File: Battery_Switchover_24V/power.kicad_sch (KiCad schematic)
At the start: 20 parts, among them U12 L5973D, U13 AMS1117-3.3

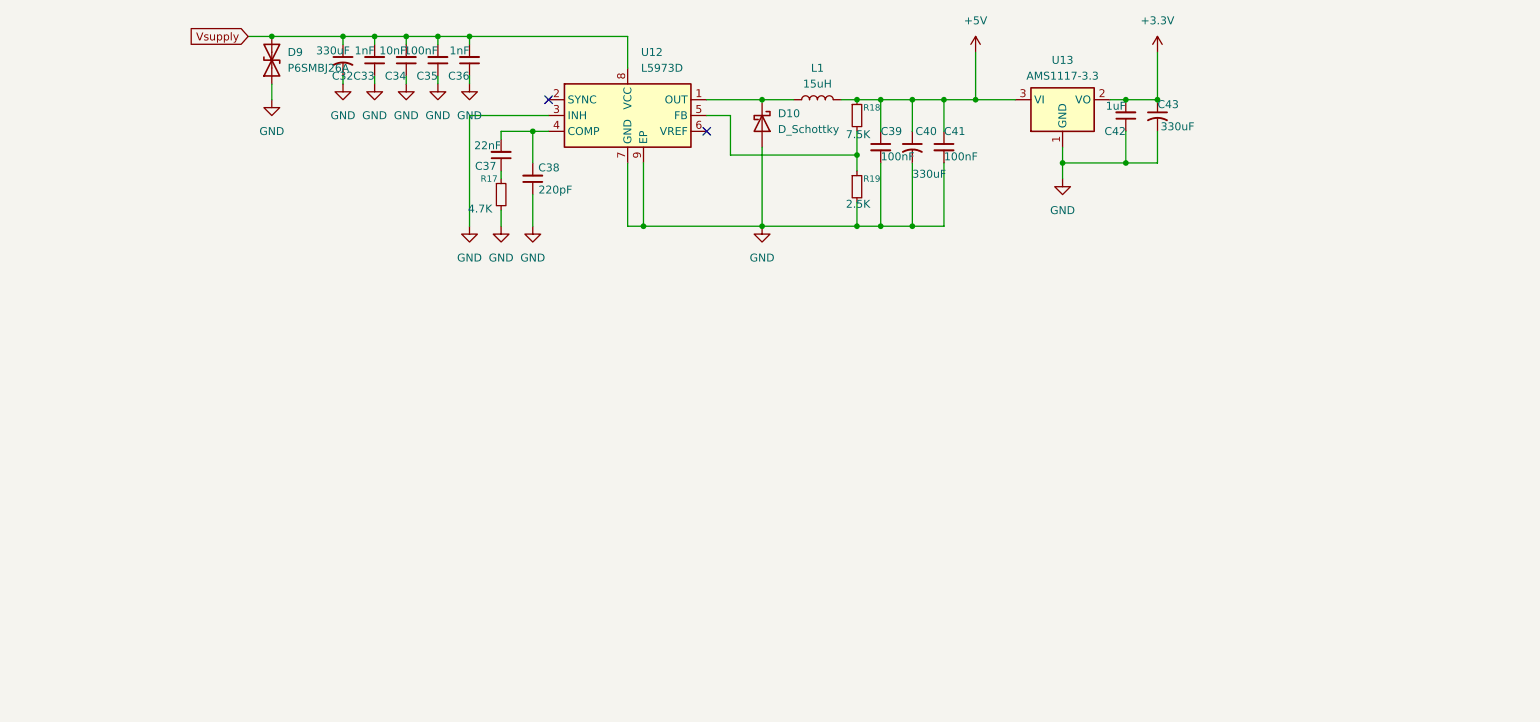
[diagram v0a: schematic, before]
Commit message: Added common mode chokes for input and output of the load fixed the corrupted board
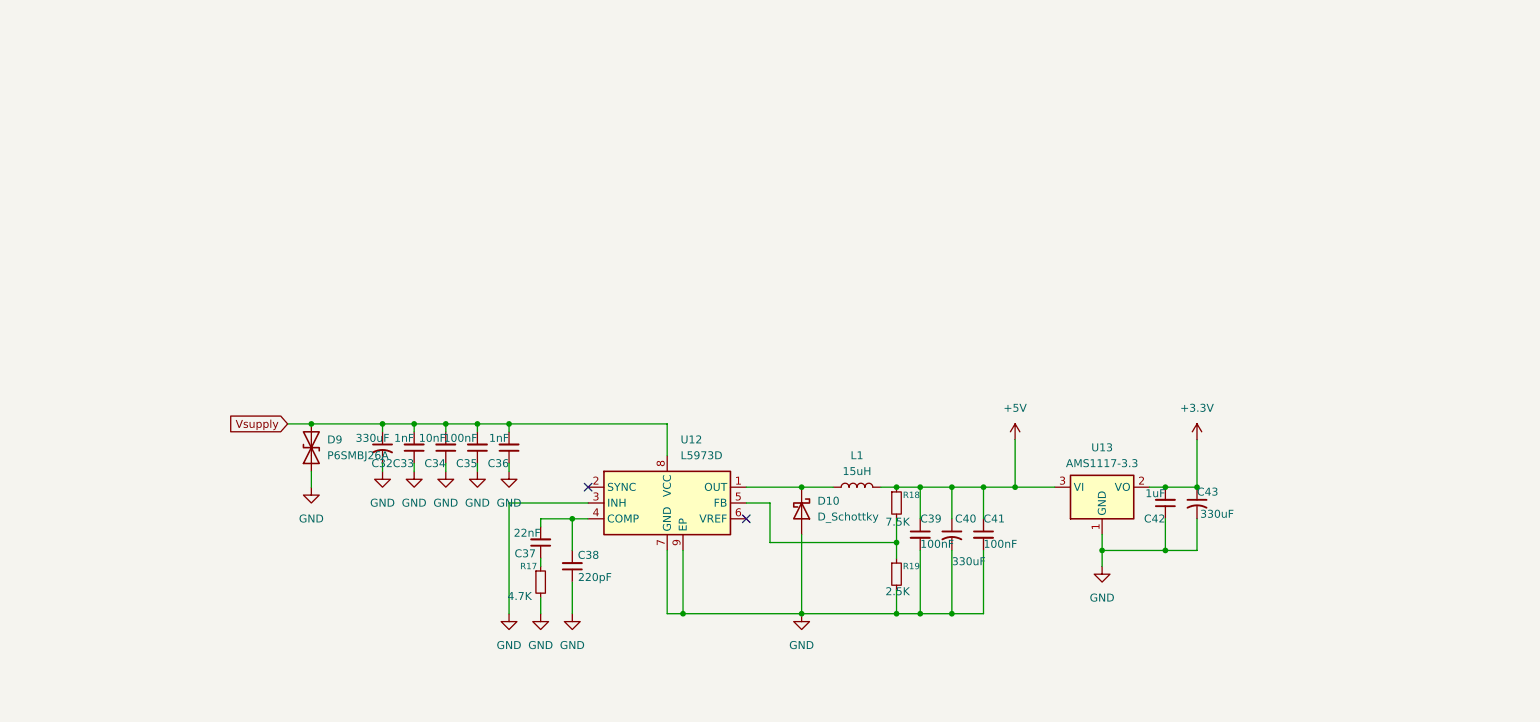
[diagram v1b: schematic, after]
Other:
- moved on the sheet: C32, C33, C34, C35, C36, C37, C38, C39, C40, C41, C42, C43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

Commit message: Added Footprints to the remaining parts calculated the current IC's resistance and capcitances
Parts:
- D10: footprint (none) -> Diode_SMD:D_SMA
- L1: footprint (none) -> footprints:IND_XAL6060_COC-L
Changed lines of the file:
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@@
 			)
 		)
-		(property "Footprint" ""
+		(property "Footprint" "footprints:IND_XAL6060_COC-L"
 			(at 161.29 113.03 0)
 			(effects
@@
 			)
 		)
-		(property "Footprint" ""
+		(property "Footprint" "Diode_SMD:D_SMA"
 			(at 152.4 116.84 0)
 			(effects
@@
 		)
 		(property "Footprint" "Capacitor_THT:CP_Radial_Tantal_D10.5mm_P5.00mm"
-			(at 85.09 106.68 0)
-			(effects
-				(font
+			(at 90.424 92.456 0)
+			(effects
+				(font

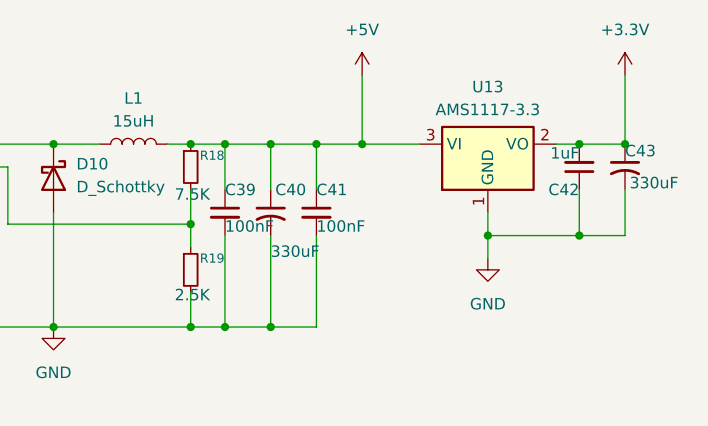
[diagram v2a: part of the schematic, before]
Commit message: Fixed opamp footprint issue done some preliminary placement
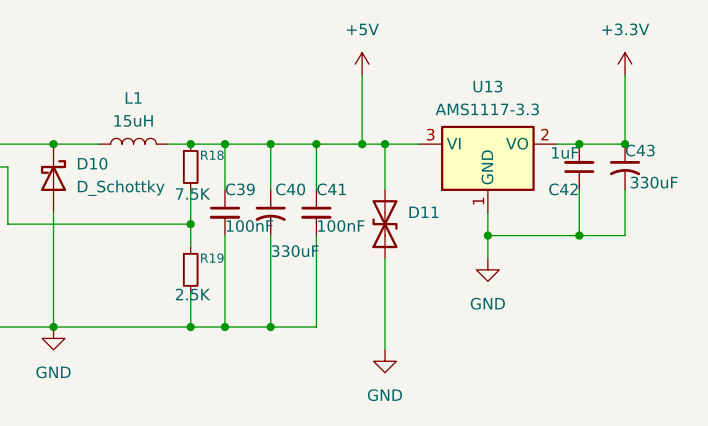
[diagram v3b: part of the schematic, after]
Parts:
- added D11: ~, footprints:P26_DO-214AA_SMB, symbol Device:D_TVS
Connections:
- net +5V: now also D11.2 (A2)
- net GND: now also D11.1 (A1)
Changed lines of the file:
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@@
+	)
+	(junction
+		(at 189.23 113.03)
+		(diameter 0)
+		(color 0 0 0 0)
 	)
 	(junction
@@
 	(wire
 		(pts
+			(xy 189.23 113.03) (xy 193.04 113.03)
+		)
+		(stroke
+			(width 0)
+			(type default)
+		)
+	)
+	(wire
+		(pts
 			(xy 167.64 121.92) (xy 167.64 124.46)
 		)
@@
 	(wire
 		(pts
-			(xy 186.69 113.03) (xy 193.04 113.03)
+			(xy 186.69 113.03) (xy 189.23 113.03)
 		)
 		(stroke
@@
 	(wire
 		(pts
+			(xy 189.23 125.73) (xy 189.23 135.89)
+		)
+		(stroke
+			(width 0)
+			(type default)
+		)
+	)
+	(wire
+		(pts
 			(xy 105.41 109.22) (xy 105.41 110.49)
 		)
@@
 		(pts
 			(xy 110.49 118.11) (xy 115.57 118.11)
+		)
+		(stroke
+			(width 0)
+			(type default)
+		)
+	)
+	(wire
+		(pts
+			(xy 189.23 113.03) (xy 189.23 118.11)
 		)
 		(stroke
@@
 	)
 	(symbol
+		(lib_id "Device:D_TVS")
+		(at 189.23 121.92 90)
+		(unit 1)
+		(exclude_from_sim no)
+		(in_bom yes)
+		(on_board yes)
+		(dnp no)
+		(fields_autoplaced yes)
+		(property "Reference" "D11"
+			(at 191.77 120.6499 90)
+			(effects
+				(font
+					(size 1.27 1.27)
+				)
+				(justify right)
+			)
+		)
+		(property "Value" "~"
+			(at 191.77 123.1899 90)
+			(effects
+				(font
+					(size 1.27 1.27)
+				)
+				(justify right)
+			)
+		)
+		(property "Footprint" "footprints:P26_DO-214AA_SMB"
+			(at 189.23 121.92 0)
+			(effects
+				(font
+					(size 1.27 1.27)
+				)
+				(hide yes)
+			)
+		)
+		(property "Datasheet" "~"
+			(at 189.23 121.92 0)
+			(effects
+				(font
+					(size 1.27 1.27)
+				)
+				(hide yes)
+			)
+		)
+		(property "Description" "Bidirectional transient-voltage-suppression diode"
+			(at 189.23 121.92 0)
+			(effects
+				(font
+					(size 1.27 1.27)
+				)
+				(hide yes)
+			)
+		)
+		(pin "2"
+		)
+		(pin "1"
+		)
+		(instances
+			(project "Battery_Switchover_24V"
+				(path "/045845e0-5d00-4da8-961e-99bdf190f683/0650697f-8d34-4346-a93f-e65dd5d58ae8"
+					(reference "D11")
+					(unit 1)
+				)
+			)
+		)
+	)
+	(symbol
 		(lib_id "power:GND")
 		(at 110.49 133.35 0)
@@
 					(unit 1)
 				)
+			)
+		)
+	)
+	(symbol
+		(lib_id "power:GND")
+		(at 189.23 135.89 0)
+		(unit 1)
+		(exclude_from_sim no)
+		(in_bom yes)
+		(on_board yes)
+		(dnp no)
+		(fields_autoplaced yes)
+		(property "Reference" "#PWR084"
+			(at 189.23 142.24 0)
+			(effects
+				(font
+					(size 1.27 1.27)
+				)
+				(hide yes)
+			)
+		)
+		(property "Value" "GND"
+			(at 189.23 140.97 0)
+			(effects
+				(font
+					(size 1.27 1.27)
+				)
+			)
+		)
+		(property "Footprint" ""
+			(at 189.23 135.89 0)
+			(effects
+				(font
+					(size 1.27 1.27)
+				)
+				(hide yes)
+			)
+		)
+		(property "Datasheet" ""
+			(at 189.23 135.89 0)
+			(effects
+				(font
+					(size 1.27 1.27)
+				)
+				(hide yes)
+			)
+		)
+		(property "Description" "Power symbol creates a global label with name \"GND\" , ground"
+			(at 189.23 135.89 0)
+			(effects
+				(font
+					(size 1.27 1.27)
+				)
+				(hide yes)
+			)
+		)
+		(pin "1"
+		)
+		(instances
+			(project "Battery_Switchover_24V"
+				(path "/045845e0-5d00-4da8-961e-99bdf190f683/0650697f-8d34-4346-a93f-e65dd5d58ae8"
+					(reference "#PWR084")
+					(unit 1)
+				)

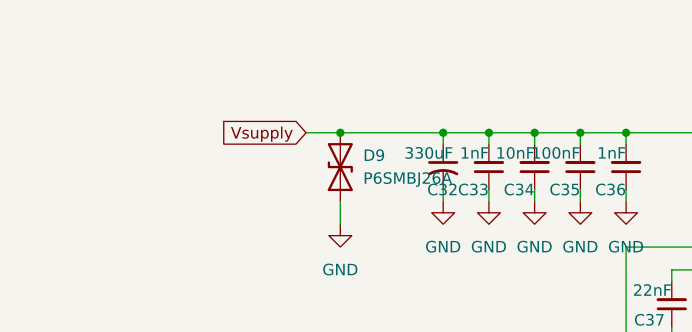
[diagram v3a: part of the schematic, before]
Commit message: Batt current monitor IC added, batt moved to charger page
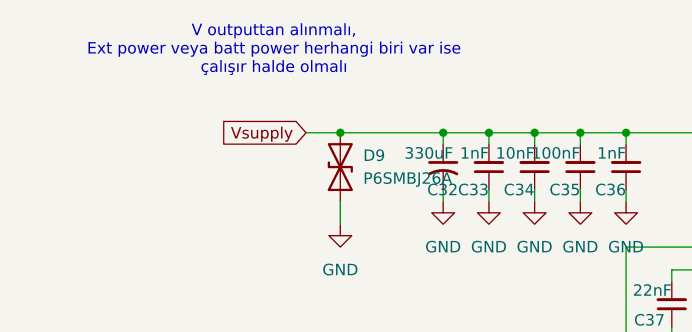
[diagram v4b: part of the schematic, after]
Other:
- note added: "V outputtan alınmalı, Ext power veya batt power herhangi biri var ise çalışır halde olmalı"
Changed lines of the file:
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@@
 	(generator_version "9.0")
 	(paper "A4")
+	(text "V outputtan alınmalı, \nExt power veya batt power herhangi biri var ise\nçalışır halde olmalı"
+		(exclude_from_sim no)
+		(at 66.294 93.726 0)
+		(effects
+			(font
+				(size 1.27 1.27)
+			)
+		)
+	)
 	(junction
 		(at 100.33 102.87)

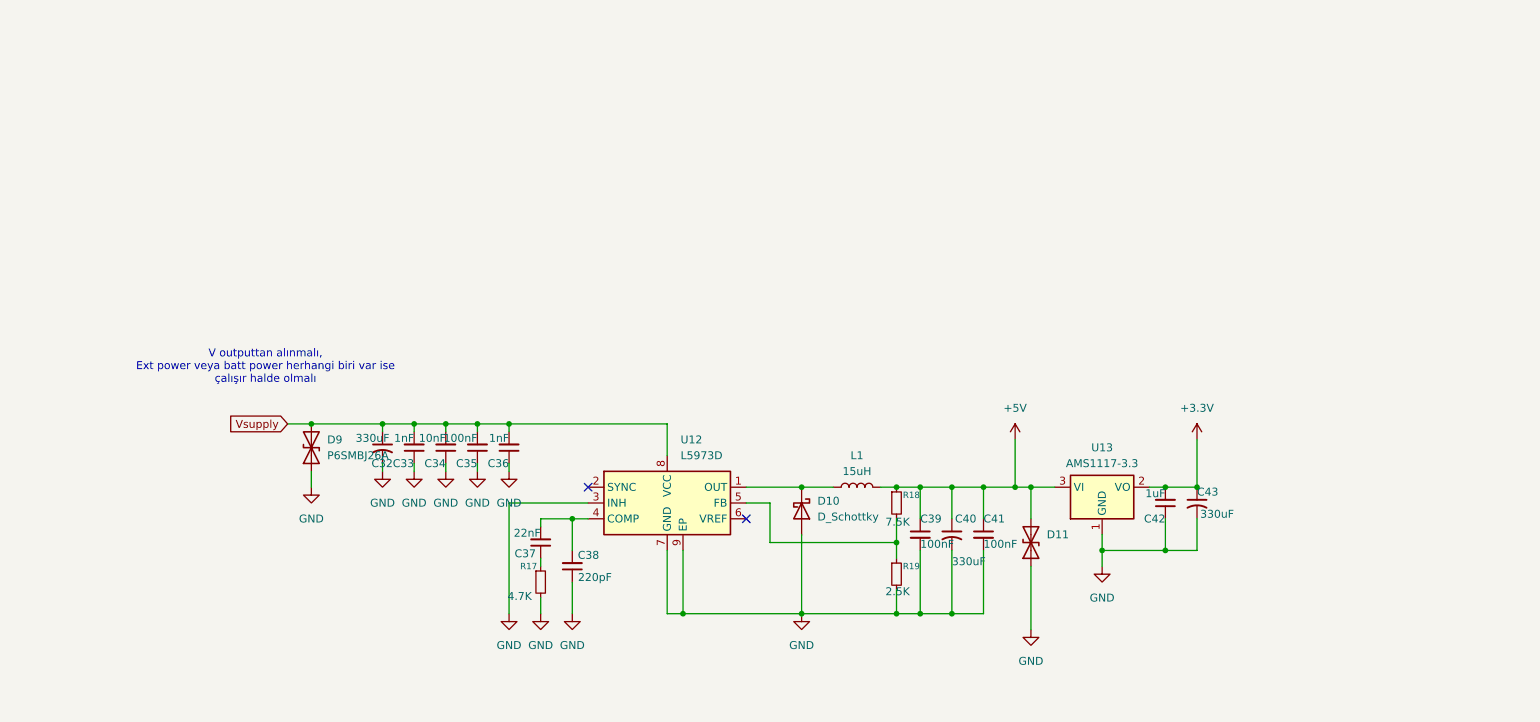
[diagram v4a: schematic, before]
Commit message: Labels assigned
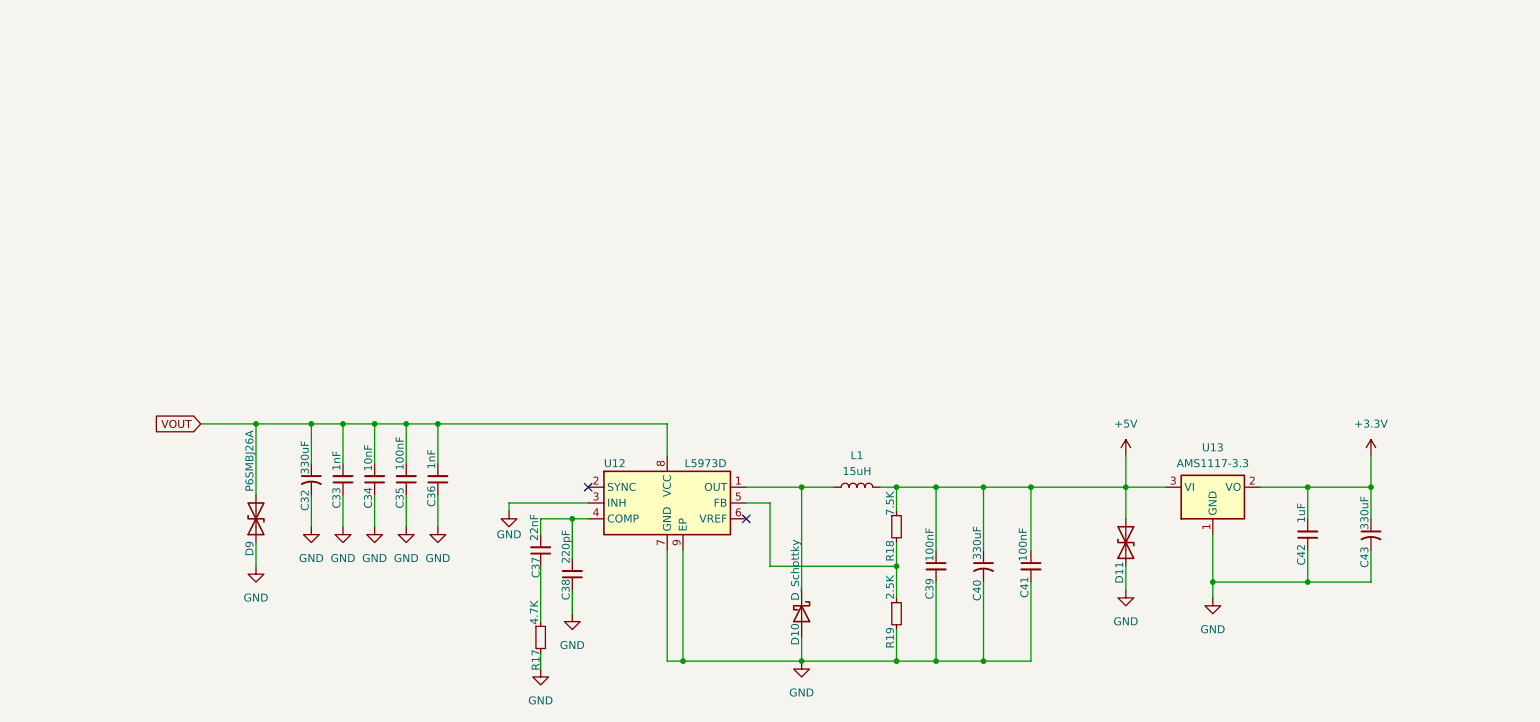
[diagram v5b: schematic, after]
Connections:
- net Vsupply renamed VOUT
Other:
- note removed: "V outputtan alınmalı, Ext power veya batt power herhangi biri var ise çalışır halde olmalı"
- moved on the sheet: C32, C33, C34, C35, C36, C37, C38, C39, C40, C41, C42, C43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

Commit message: Cap FP, Choke FP, Ind FP added. Basic locations
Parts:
- C32, C40, C43: footprint Capacitor_THT:CP_Radial_Tantal_D10.5mm_P5.00mm -> Capacitor_SMD:CP_Elec_8x10
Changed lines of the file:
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@@
 			)
 		)
-		(property "Footprint" "Capacitor_THT:CP_Radial_Tantal_D10.5mm_P5.00mm"
+		(property "Footprint" "Capacitor_SMD:CP_Elec_8x10"
 			(at 243.84 120.65 0)
 			(effects
@@
 			)
 		)
-		(property "Footprint" "Capacitor_THT:CP_Radial_Tantal_D10.5mm_P5.00mm"
+		(property "Footprint" "Capacitor_SMD:CP_Elec_8x10"
 			(at 181.61 125.73 0)
 			(effects
@@
 			)
 		)
-		(property "Footprint" "Capacitor_THT:CP_Radial_Tantal_D10.5mm_P5.00mm"
+		(property "Footprint" "Capacitor_SMD:CP_Elec_8x10"
 			(at 78.994 97.536 0)
 			(effects

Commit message: Board turned to horizontal
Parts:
- added C67: 10uF 50V X7R, Capacitor_SMD:C_1206_3216Metric, symbol Device:C_Small
- added C68, C69: 10uF 16V X7R, Capacitor_SMD:C_1206_3216Metric, symbol Device:C_Small
- C33: value 1nF -> 10uF 50V X7R; footprint Capacitor_SMD:C_0402_1005Metric -> Capacitor_SMD:C_1206_3216Metric
- C34: value 10nF -> 10uF 50V X7R; footprint Capacitor_SMD:C_0603_1608Metric -> Capacitor_SMD:C_1206_3216Metric
- C35: value 100nF -> 10uF 50V X7R; footprint Capacitor_SMD:C_0603_1608Metric -> Capacitor_SMD:C_1206_3216Metric
- C36: value 1nF -> 100nF
- C37, C38: footprint Capacitor_SMD:C_0402_1005Metric -> Capacitor_SMD:C_0603_1608Metric
- C39: value 100nF -> 100nF 16V; footprint Capacitor_SMD:C_0603_1608Metric -> Capacitor_SMD:C_1206_3216Metric
- C41: value 100nF -> 10uF 16V X7R; footprint Capacitor_SMD:C_0603_1608Metric -> Capacitor_SMD:C_1206_3216Metric
- C42: footprint Capacitor_SMD:C_0603_1608Metric -> Capacitor_SMD:C_0805_2012Metric
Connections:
- net +5V: now also C41.2, C68.2, C69.2; no longer C41.1
- net GND: now also C41.1, C67.1, C68.1, C69.1; no longer C41.2
- net VOUT: now also C67.2
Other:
- moved on the sheet: C32, C33, C36, C42, C43, D11, D9, U13

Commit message: Routing
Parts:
- removed D9: P6SMBJ26A, footprints:P26_DO-214AA_SMB, symbol Device:D_TVS
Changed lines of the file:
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@@
-	)
-	(junction
-		(at 43.18 102.87)
-		(diameter 0)
-		(color 0 0 0 0)
 	)
 	(junction
@@
 	(wire
 		(pts
-			(xy 34.29 102.87) (xy 43.18 102.87)
-		)
-		(stroke
-			(width 0)
-			(type default)
-		)
-	)
-	(wire
-		(pts
 			(xy 76.2 109.22) (xy 76.2 102.87)
 		)
@@
 	(wire
 		(pts
-			(xy 43.18 102.87) (xy 48.26 102.87)
+			(xy 34.29 102.87) (xy 48.26 102.87)
 		)
 		(stroke
@@
 	(wire
 		(pts
-			(xy 43.18 121.92) (xy 43.18 125.73)
-		)
-		(stroke
-			(width 0)
-			(type default)
-		)
-	)
-	(wire
-		(pts
 			(xy 255.27 123.19) (xy 255.27 128.27)
 		)
@@
 		(pts
 			(xy 48.26 102.87) (xy 48.26 109.22)
-		)
-		(stroke
-			(width 0)
-			(type default)
-		)
-	)
-	(wire
-		(pts
-			(xy 43.18 114.3) (xy 43.18 102.87)
 		)
 		(stroke
@@
 	(symbol
 		(lib_id "Device:D_TVS")
-		(at 43.18 118.11 90)
-		(unit 1)
-		(exclude_from_sim no)
-		(in_bom yes)
-		(on_board yes)
-		(dnp no)
-		(property "Reference" "D9"
-			(at 42.164 121.666 0)
-			(effects
-				(font
-					(size 1.27 1.27)
-				)
-				(justify right)
-			)
-		)
-		(property "Value" "P6SMBJ26A"
-			(at 42.164 103.886 0)
-			(effects
-				(font
-					(size 1.27 1.27)
-				)
-				(justify right)
-			)
-		)
-		(property "Footprint" "footprints:P26_DO-214AA_SMB"
-			(at 43.18 118.11 0)
-			(effects
-				(font
-					(size 1.27 1.27)
-				)
-				(hide yes)
-			)
-		)
-		(property "Datasheet" "~"
-			(at 43.18 118.11 0)
-			(effects
-				(font
-					(size 1.27 1.27)
-				)
-				(hide yes)
-			)
-		)
-		(property "Description" "Bidirectional transient-voltage-suppression diode"
-			(at 43.18 118.11 0)
-			(effects
-				(font
-					(size 1.27 1.27)
-				)
-				(hide yes)
-			)
-		)
-		(pin "2"
-		)
-		(pin "1"
-		)
-		(instances
-			(project "Battery_Switchover_24V"
-				(path "/045845e0-5d00-4da8-961e-99bdf190f683/0650697f-8d34-4346-a93f-e65dd5d58ae8"
-					(reference "D9")
-					(unit 1)
-				)
-			)
-		)
-	)
-	(symbol
-		(lib_id "Device:D_TVS")
 		(at 226.06 121.92 90)
 		(unit 1)
@@
 					(unit 1)
 				)
-			)
-		)
-	)
-	(symbol
-		(lib_id "power:GND")
-		(at 43.18 125.73 0)
-		(unit 1)
-		(exclude_from_sim no)
-		(in_bom yes)
-		(on_board yes)
-		(dnp no)
-		(fields_autoplaced yes)
-		(property "Reference" "#PWR060"
-			(at 43.18 132.08 0)
-			(effects
-				(font
-					(size 1.27 1.27)
-				)
-				(hide yes)
-			)
-		)
-		(property "Value" "GND"
-			(at 43.18 130.81 0)
-			(effects
-				(font
-					(size 1.27 1.27)
-				)
-			)
-		)
-		(property "Footprint" ""
-			(at 43.18 125.73 0)
-			(effects
-				(font
-					(size 1.27 1.27)
-				)
-				(hide yes)
-			)
-		)
-		(property "Datasheet" ""
-			(at 43.18 125.73 0)
-			(effects
-				(font
-					(size 1.27 1.27)
-				)
-				(hide yes)
-			)
-		)
-		(property "Description" "Power symbol creates a global label with name \"GND\" , ground"
-			(at 43.18 125.73 0)
-			(effects
-				(font
-					(size 1.27 1.27)
-				)
-				(hide yes)
-			)
-		)
-		(pin "1"
-		)
-		(instances
-			(project "Battery_Switchover_24V"
-				(path "/045845e0-5d00-4da8-961e-99bdf190f683/0650697f-8d34-4346-a93f-e65dd5d58ae8"
-					(reference "#PWR060")
-					(unit 1)
-				)
